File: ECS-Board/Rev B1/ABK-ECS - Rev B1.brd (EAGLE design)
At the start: 100 x 100 mm, 298 parts, among them J1 USB-B-S-RA, J10 FTSH-105-01-L-DV-NOPASTE, J11 22-05-7028-02, J12 RB1-125BAG1A, J13 22-05-7068-06, J14 22-05-7048-04, J15 22-05-7048-04, J16 22-05-7048-04, J2 MSTBA2, J3 22-05-7068-06, J5 22-05-7068-06, J6 22-05-7068-06, J7 22-05-7068-06, J8 22-05-7028-02, J9 FTSH-103-01-L-DV-NOPASTE, SW1 B3FS-1015, SW2 B3FS-1015, T1 MMBT2907ALT3, T10 MMBT2222AL, T11 IRLML5103TRPBF, T12 MMBT2222AL, T13 IRLML5103TRPBF, T14 IRLML5103TRPBF, T15 IRLML5103TRPBF, T16 IRLML5103TRPBF, T17 MMBT2222AL, T18 MMBT2222AL, T19 MMBT2222AL, T2 EXMACHINA-LOGO-NAME, T20 MMBT2222AL, T3 IRLML5103TRPBF, T4 IRLML5103TRPBF, T5 IRLML5103TRPBF, T6 IRLML5103TRPBF, T7 MMBT2222AL, T8 MMBT2222AL, T9 MMBT2222AL, U1 AT24C512C-SSHM-B, U10 SN74LVC2G17DBVR, U2 LPC1768FBD100, U3 LT3686HDDPBF, U4 LT3686HDDPBF, U5 CD4050BD, U6 CD4050BD, U7 DP83848JSQ/NOPB, U9 SN74LVC2G17DBVR, X1 FC-135, X2 ASE-12, X3 3000, X4 ASE_50

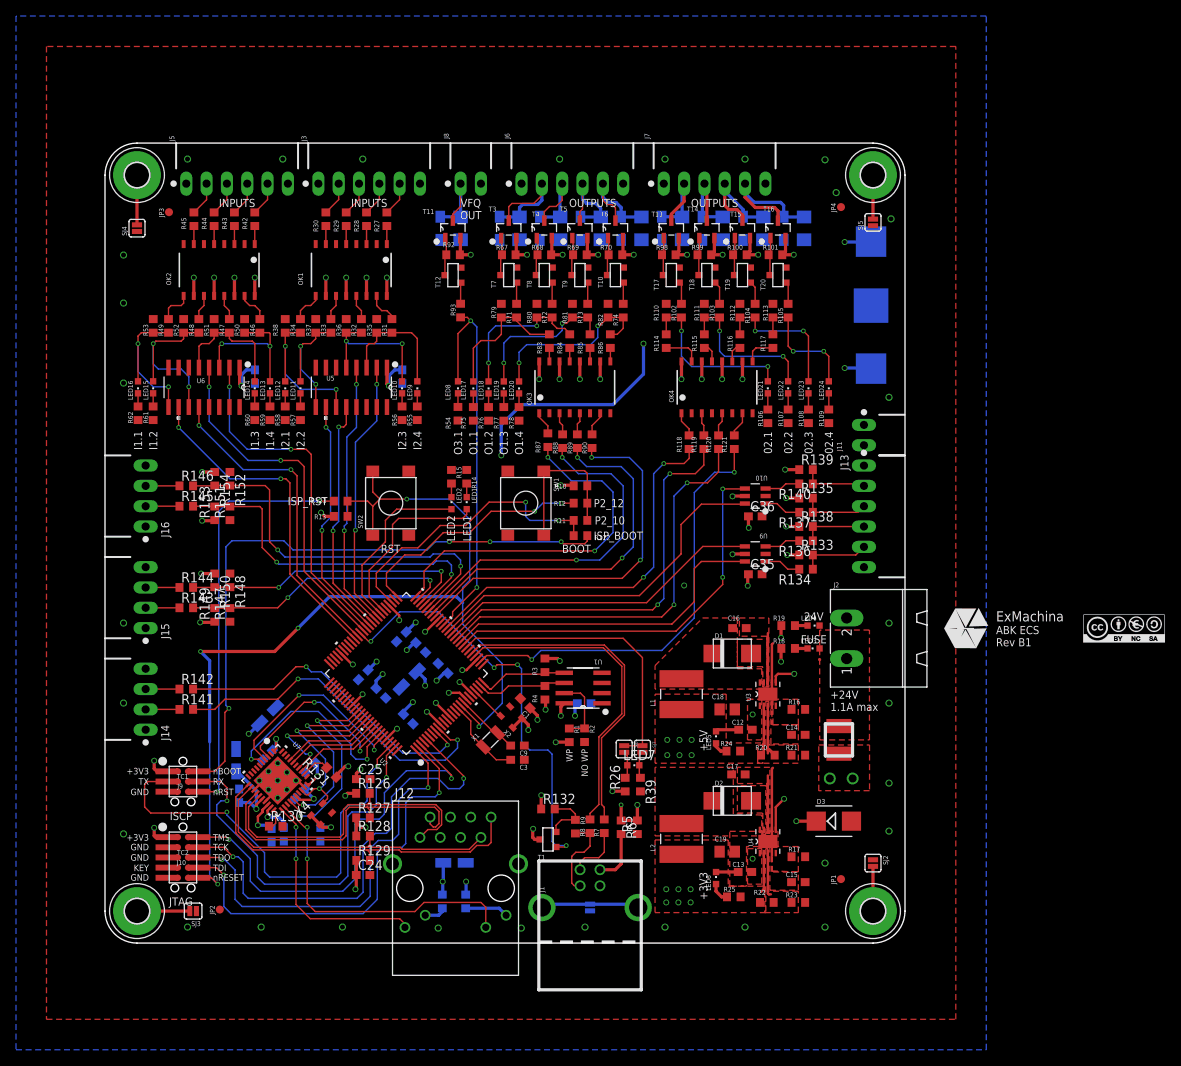
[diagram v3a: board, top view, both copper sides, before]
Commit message: Improte routing and add Silkscreen
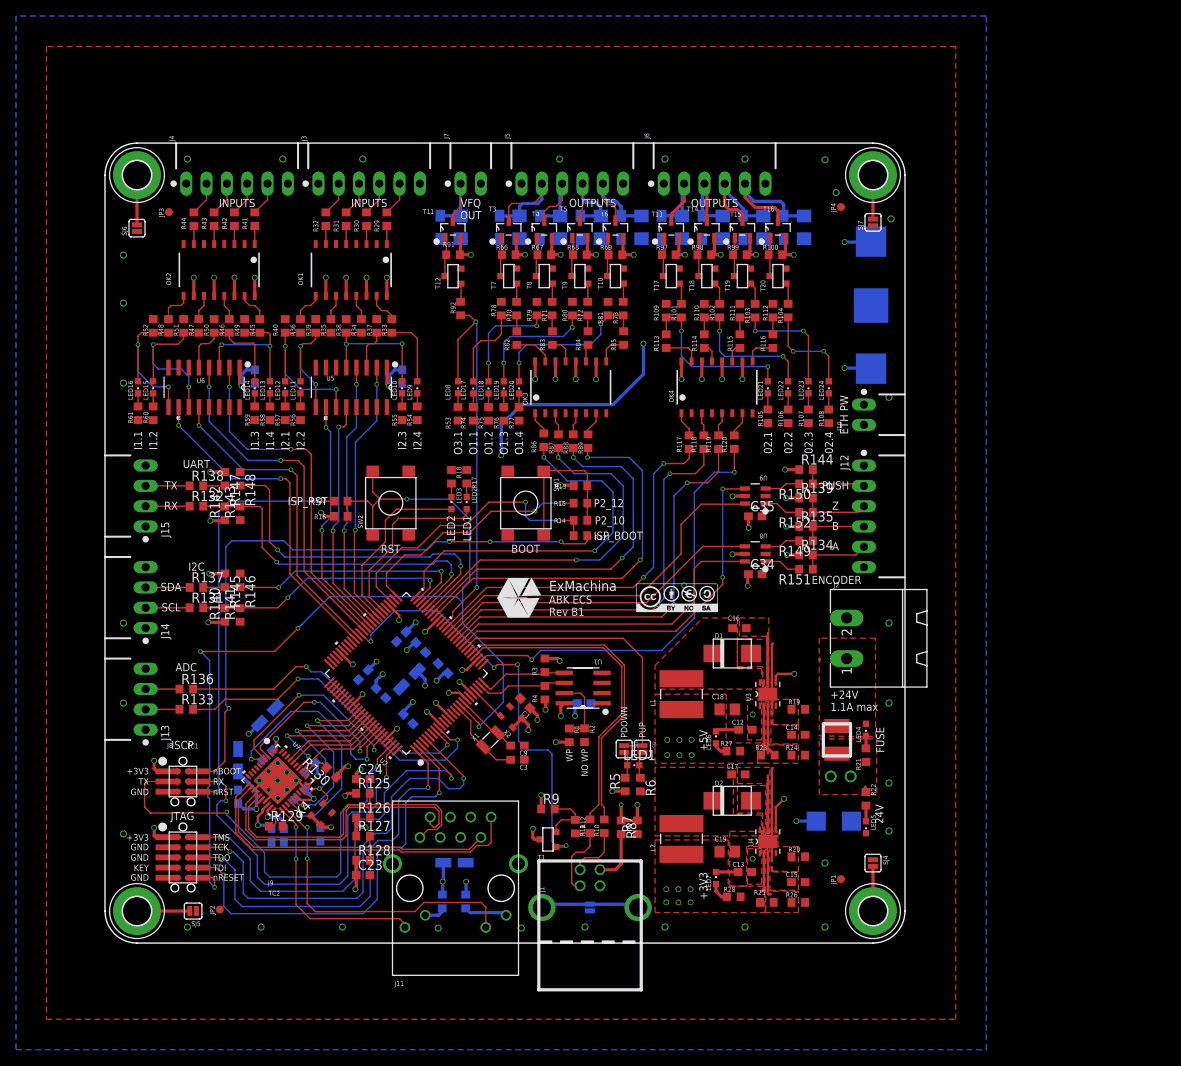
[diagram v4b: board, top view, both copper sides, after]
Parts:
- removed C36: 0.1uF, rcl:C0603
- removed D13: 1N4148WS, diode:SOD323-W
- removed J16: 22-05-7048-04, con-molex:7395-04
- removed R153, R154: 1K, rcl:R0603
- removed U10: SN74LVC2G17DBVR, ti:SOT95P280X145-6N
- added C20: 0.1uF, rcl:C0603
- added D4: 1N4148WS, diode:SOD323-W
- added J4: 22-05-7068-06, con-molex:7395-06
- added R40: 4K7, rcl:R0603
- added R41: 1K, rcl:R0603
- added U8: SN74LVC2G17DBVR, ti:SOT95P280X145-6N
- C22: value 0.1uF -> 4.7uF; device rcl:C0603 -> rcl:CT3216
- C23: value 4.7uF -> 100nF; device rcl:CT3216 -> rcl:C0603
- C25, C29: value 100nF -> 10uF; device rcl:C0603 -> rcl:CT3216
- C26, C30: value 10uF -> 100nF; device rcl:CT3216 -> rcl:C0603
- C34: value 100nF -> 0.1uF
- J10: value FTSH-105-01-L-DV-NOPASTE -> 22-05-7028-02; device con-samtec:FTSH-105-01-L-DV-NOPASTE -> con-molex:7395-02
- J11: value 22-05-7028-02 -> RB1-125BAG1A; device con-molex:7395-02 -> con-wiznet:WIZNET_RB1-125BAG1A
- J12: value RB1-125BAG1A -> 22-05-7068-06; device con-wiznet:WIZNET_RB1-125BAG1A -> con-molex:7395-06
- J13: value 22-05-7068-06 -> 22-05-7048-04; device con-molex:7395-06 -> con-molex:7395-04
- J7: value 22-05-7068-06 -> 22-05-7028-02; device con-molex:7395-06 -> con-molex:7395-02
- J8: value 22-05-7028-02 -> FTSH-103-01-L-DV-NOPASTE; device con-molex:7395-02 -> con-samtec:FTSH-103-01-L-DV-NOPASTE
- J9: value FTSH-103-01-L-DV-NOPASTE -> FTSH-105-01-L-DV-NOPASTE; device con-samtec:FTSH-103-01-L-DV-NOPASTE -> con-samtec:FTSH-105-01-L-DV-NOPASTE
- LED3: value Red -> Blue
- LED4: value Blue -> Red
- MP1, MP2, MP3, MP4: value MOUNT-PAD3,0 -> MOUNT-PAD3.5; device holes:P3,0 -> holes:P3,5
- R10: value 10K -> 33
- R101, R70: value 10K -> 1K
- R105, R27, R28, R74: value 1K -> 1K5
- R109, R39, R78: value 1K5 -> 4K7
- R11: value 0R -> 33
- R113, R82: value 4K7 -> 100
- R117, R86: value 100 -> 330
- R12: value 0R -> 1K5
- R121: value 330 -> 0R
- R123: value 0R -> 220
- R125: value 220 -> 49.9
- R129: value 49.9 -> 4K7
- R130: value 4K7 -> 2K2
- R131: value 2K2 -> 1K
- R132: value 0R, DNI -> 1K
- R133, R138, R35, R36: value 4K7 -> 1K
- R134, R144, R49: value 1K -> 4K7
- R14, R15: value 1K5 -> 0R
- R16: value 31K6 -> 10K
- R17: value 31K6 -> 1K5
- R18, R53: value 4K7 -> 1K5
- R19: value 4K7 -> 31K6
- R20: value 52K3 -> 31K6
- R21: value 10K -> 4K7
- R22: value 31K6 -> 4K7
- R23: value 10K -> 52K3
- R24, R26: value 1K5 -> 10K
- R25: value 1K5 -> 31K6
- R5: value 39K -> 1K5
- R6: value 24K -> 1K5
- R62: value 1K5 -> 1K; device rcl:R0603 -> rcl:R1206
- R66, R91, R97: value 1K -> 10K; device rcl:R1206 -> rcl:R0603
- R7: value 33 -> 39K
- R8: value 33 -> 24K
- R9: value 1K5 -> 0R, DNI
- R90: value 330 -> 1K; device rcl:R0603 -> rcl:R1206
- R92: value 10K -> 100
- R93: value 100 -> 1K; device rcl:R0603 -> rcl:R1206
- SJ1: value (none) -> SJNC
- SJ2, SJ3, SJ4, SJ5: value SOLDERJUMPERNC -> SJNC
- moved SJ4 121.5 mm to (96.0, 10.0), turned to 270 degrees
- moved SJ5 121.0 mm to (11.0, 4.00), turned to 180 degrees
- moved J10 101.5 mm to (94.9, 66.0), turned to 90 degrees
- moved R28 96.3 mm to (78.6, 5.78), turned to 0 degrees
- moved J13 92.7 mm to (5.08, 30.5), turned to 270 degrees
- moved SJ6 89.1 mm to (4.00, 89.4), turned to 90 degrees
- moved J8 82.9 mm to (9.74, 20.2), turned to 270 degrees
- moved R133 79.8 mm to (10.2, 29.2)
- moved R136 79.7 mm to (10.2, 31.8), turned to 0 degrees
- moved R27 79.3 mm to (78.5, 24.0), turned to 0 degrees
- moved R144 78.9 mm to (87.6, 59.2)
- moved R137 76.8 mm to (11.4, 44.5), turned to 0 degrees
- moved R138 76.4 mm to (11.4, 57.1)
- moved J11 76.3 mm to (43.8, 6.86), turned to 0 degrees
- moved R150 74.9 mm to (87.6, 57.4), turned to 180 degrees
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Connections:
- removed net N$3 (its old number): LED2.C, R15.1
- new net N$45: LED4.C, R21.1
- net !ISP_BOOT: now also J8.2, R121.2; no longer J9.2, R122.2
- net !ISP_RST: now also J8.6, R122.2; no longer J9.6, R123.2
- net !RESET: now also J9.10, R122.1, R16.1; no longer J10.10, R123.1, R13.1
- net +24V: now also J4.1, R21.2, R22.2, R66.2, R91.2, R97.2; no longer J7.1, R101.2, R18.2, R19.2, R70.2, R92.2
- net +3V3: now also C20.1, C22.+, C23.1, C29.+, C30.1, J11.R3, J14.1, J8.1, R123.2, R125.1, R130.1, R140.1, R142.1, R145.1, R147.1, R16.2, R28.2, R5.1, R9.1, U8.5; no longer C22.1, C23.+, C25.1, C30.+, C36.1, J10.1, J12.R3, J16.1, R10.2, R125.2, R129.1, R131.1, R132.1, R149.1, R150.1, R153.1, R154.1, R22.2, R26.1, U10.5
- net +5V: now also J10.1, J12.1, R134.1, R144.1, R23.2, R27.2; no longer J11.1, J13.6, R133.1, R138.1, R20.2, R24.2
- net 1: now also SJ4.2; no longer SJ2.2
- net 2: now also SJ5.2; no longer SJ3.2
- net 3: now also SJ6.2; no longer SJ4.2
- net 4: now also SJ7.2; no longer SJ5.2
- net ADC1: now also R136.2; no longer R142.2
- net ADC2: now also R133.2; no longer R141.2
- net AGND: now also J11.S1, J11.S2; no longer J12.S1, J12.S2
- net BOOT_SELECT_P2_10: now also R121.1, R14.1; no longer R11.1, R122.1
- net BOOT_SELECT_P2_12: now also R15.1; no longer R12.1
- net ENCODER_A: now also U8.6; no longer U9.6
- net ENCODER_B: now also U8.4; no longer U9.4
- net ENCODER_PUSH: now also U9.4; no longer U10.4
- net ENCODER_Z: now also U9.6; no longer U10.6
- net ETH_RX_N: now also J11.R8, R128.2; no longer J12.R8, R129.2
- net ETH_RX_P: now also J11.R7, R127.2; no longer J12.R7, R128.2
- net ETH_TX_N: now also J11.R2, R126.2; no longer J12.R2, R127.2
- net ETH_TX_P: now also J11.R1, R125.2; no longer J12.R1, R126.2
- net GND: now also C20.2, C22.-, C23.2, C25.-, C26.2, C29.-, C30.2, D4.A, J10.2, J11.R4, J11.R5, J11.R6, J12.6, J13.4, J4.6, J7.2, J8.5, J9.3, J9.7, J9.9, LED7.C, R105.2, R129.2, R141.1, R143.1, R146.1, R17.2, R18.2, R19.1, R20.1, R24.1, R26.1, R40.2, R49.2, R6.2, R62.1, R7.1, R74.2, R90.1, R93.1, SJ6.1, SJ7.1, U8.2; no longer C22.2, C23.-, C25.2, C26.-, C29.2, C30.-, C36.2, D13.A, J10.3, J10.5, J10.7, J10.9, J11.2, J12.R4, J12.R5, J12.R6, J13.1, J16.4, J7.6, J8.2, LED4.C, R113.2, R130.2, R14.2, R147.1, R15.2, R151.1, R152.1, R16.1, R17.1, R21.1, R23.1, R35.2, R36.2, R5.1, R62.2, R66.1, R82.2, R91.1, R97.1, SJ1.1, SJ2.1, U10.2
- net I2C_SCL: now also R131.2, R140.2, R141.2; no longer R143.2, R147.2, R149.2
- net I2C_SDA: now also R137.2, R145.2, R146.2; no longer R144.2, R148.2, R150.2
- net INPUT1.1: now also R48.2, R52.1; no longer R49.2, R53.1
- net INPUT1.2: now also R47.2, R51.1; no longer R48.2, R52.1
- net INPUT1.3: now also R46.2, R50.1; no longer R47.2, R51.1
- net INPUT1.4: now also R45.2, R49.1; no longer R46.2, R50.1
- net INPUT2.1: now also R36.2, R40.1; no longer R34.2, R38.1
- net INPUT2.2: now also R35.2, R39.1; no longer R33.2, R37.1
- net INPUT2.3: now also R34.2, R38.1; no longer R32.2, R36.1
- net INPUT2.4: now also R33.2, R37.1; no longer R31.2, R35.1
- net ISP_RXDO: now also J8.4; no longer J9.4
- net ISP_TXDO: now also J8.3; no longer J9.3
- net JTAG_TCK: now also J9.4; no longer J10.4
- net JTAG_TDI: now also J9.8; no longer J10.8
- net JTAG_TDO: now also J9.6; no longer J10.6
- net JTAG_TMS: now also J9.2; no longer J10.2
- net L1_1: now also J11.L2; no longer J12.L2
- net L1_2: now also J11.L4; no longer J12.L4
- net MII_MODE: now also R130.2; no longer R131.2
- net MOTOR_VFQ: now also D8.C, J7.1, R90.2; no longer D9.C, J8.1, R91.2
- net N$1: now also R11.1, R12.2; no longer R8.1, R9.2
- net N$100: now also R45.1; no longer R46.1
- net N$101: now also R42.2; no longer R43.2
- net N$102: now also J4.4, R42.1; no longer J5.4, R43.1
- net N$103: now also R46.1; no longer R47.1
- net N$104: now also R43.2; no longer R44.2
- net N$105: now also J4.3, R43.1; no longer J5.3, R44.1
- net N$106: now also R47.1; no longer R48.1
- net N$107: now also R58.1; no longer R59.1
- net N$108: now also R59.1; no longer R60.1
- net N$109: now also R60.1; no longer R61.1
- net N$110: now also R48.1; no longer R49.1
- net N$111: now also R44.2; no longer R45.2
- net N$112: now also J4.2, R44.1; no longer J5.2, R45.1
- net N$113: now also J11.L1, R123.1; no longer J12.L1, R124.1
- net N$114: now also R8.2; no longer R6.2
- net N$115: now also J11.L3, R124.1; no longer J12.L3, R125.1
- net N$116: now also R129.1; no longer R130.1
- net N$117: now also J12.5, R134.2, R151.1; no longer J13.5, R133.2, R134.1
- net N$118: now also J12.4, R135.2, R149.1; no longer J13.4, R136.1, R138.2
- net N$119: now also J12.3, R139.2, R152.1; no longer J13.3, R135.2, R137.1
- net N$120: now also R150.2, U9.3; no longer R140.2, U10.3
- net N$121: now also R149.2, U8.3; no longer R136.2, U9.3
- net N$122: now also R151.2, U8.1; no longer R134.2, U9.1
- net N$123: now also R152.2, U9.1; no longer R137.2, U10.1
- net N$124: now also J12.2, R144.2, R150.1; no longer J13.2, R139.2, R140.1
- net N$125: now also J13.2, R133.1; no longer J14.2, R141.1
- net N$126: now also J13.3, R136.1; no longer J14.3, R142.1
- net N$127: now also J14.2, R131.1; no longer J15.2, R143.1
- net N$128: now also J14.3, R137.1; no longer J15.3, R144.1
- net N$129: now also J15.2, R132.1; no longer J16.2, R145.1
- net N$13: now also R25.1, R26.2; no longer R22.1, R23.2
- net N$130: now also J15.3, R138.1; no longer J16.3, R146.1
- net N$17: now also R101.2; no longer R102.2
- net N$18: now also R97.1; no longer R98.1
- net N$19: now also R102.2; no longer R103.2
- net N$2: now also R10.1; no longer R7.1
- net N$20: now also R98.1; no longer R99.1
- net N$21: now also R103.2; no longer R104.2
- net N$22: now also R99.1; no longer R100.1
- net N$23: now also R104.2; no longer R105.2
- net N$24: now also R100.1; no longer R101.1
- net N$25: now also R92.1; no longer R93.1
- net N$26: now also R91.1; no longer R92.1
- net N$28: now also LED1.A, R5.2, SJ1.2; no longer LED7.A, R26.2, SJ6.2
- net N$29: now also LED2.C, R17.1; no longer LED1.C, R14.1
- net N$30: now also R12.1, R9.2; no longer R132.2, R9.1
- net N$31: now also R70.1, R78.1, R82.1; no longer R71.1, R79.1, R83.1
- net N$32: now also LED1.C, R6.1, SJ2.2; no longer LED7.C, R39.1, SJ7.2
- net N$33: now also R82.2; no longer R83.2
- net N$34: now also R71.1, R79.1, R83.1; no longer R72.1, R80.1, R84.1
- net N$35: now also R83.2; no longer R84.2
- net N$36: now also R72.1, R80.1, R84.1; no longer R73.1, R81.1, R85.1
- net N$37: now also R73.1, R81.1, R85.1; no longer R74.1, R82.1, R86.1
- net N$38: now also R84.2; no longer R85.2
- net N$39: now also R85.2; no longer R86.2
- net N$4: now also R19.2; no longer R16.2
- net N$40: now also R86.1; no longer R87.1
- net N$41: now also R29.2; no longer R27.2
- net N$42: now also R87.1; no longer R88.1
- net N$43: now also R89.1; no longer R90.1
- net N$44: now also LED5.A, R22.1; no longer LED4.A, R19.1
- net N$46: now also R88.1; no longer R89.1
- net N$47: now also R30.2; no longer R28.2
- net N$48: now also R31.2; no longer R29.2
- net N$49: now also R32.2; no longer R30.2
- net N$5: now also R13.1, R14.2, R15.2; no longer R10.1, R11.2, R12.2
- net N$50: now also LED7.A, R28.1; no longer LED6.A, R25.1
- net N$51: now also LED6.A, R27.1; no longer LED5.A, R24.1
- net N$52: now also R32.1; no longer R30.1
- net N$53: now also R31.1; no longer R29.1
- net N$54: now also R30.1; no longer R28.1
- net N$55: now also R29.1; no longer R27.1
- net N$56: now also R53.1; no longer R54.1
- net N$57: now also R54.1; no longer R55.1
- net N$58: now also R55.1; no longer R56.1
- net N$59: now also R56.1; no longer R57.1
- net N$61: now also R36.1; no longer R34.1
- net N$62: now also R35.1; no longer R33.1
- net N$63: now also R34.1; no longer R32.1
- net N$64: now also R33.1; no longer R31.1
- net N$65: now also R57.1; no longer R58.1
- net N$66: now also R74.1; no longer R75.1
- net N$67: now also R75.1; no longer R76.1
- net N$68: now also R76.1; no longer R77.1
- net N$69: now also R77.1; no longer R78.1
- net N$7: now also R20.2; no longer R17.2
- net N$70: now also SJ3.2; no longer SJ1.2
- net N$71: now also R66.1; no longer R67.1
- net N$72: now also R67.1; no longer R68.1
- net N$75: now also R101.1, R109.1, R113.1; no longer R102.1, R110.1, R114.1
- net N$76: now also R113.2; no longer R114.2
- net N$77: now also R68.1; no longer R69.1
- net N$78: now also R69.1; no longer R70.1
- net N$79: now also R102.1, R110.1, R114.1; no longer R103.1, R111.1, R115.1
- net N$80: now also R114.2; no longer R115.2
- net N$81: now also R41.2; no longer R42.2
- net N$82: now also J4.5, R41.1; no longer J5.5, R42.1
- net N$83: now also R103.1, R111.1, R115.1; no longer R104.1, R112.1, R116.1
- net N$84: now also R70.2; no longer R71.2
- net N$85: now also R71.2; no longer R72.2
- net N$86: now also R104.1, R112.1, R116.1; no longer R105.1, R113.1, R117.1
- net N$87: now also R115.2; no longer R116.2
- net N$88: now also R116.2; no longer R117.2
- net N$89: now also R117.1; no longer R118.1
- net N$9: now also R23.1, R24.2; no longer R20.1, R21.2
- net N$90: now also R61.1; no longer R62.1
- net N$91: now also R118.1; no longer R119.1
- net N$92: now also R120.1; no longer R121.1
- net N$93: now also R119.1; no longer R120.1
- net N$94: now also R105.1; no longer R106.1
- net N$95: now also R106.1; no longer R107.1
- net N$96: now also R107.1; no longer R108.1
- net N$97: now also R108.1; no longer R109.1
- net N$98: now also R72.2; no longer R73.2
- net N$99: now also R73.2; no longer R74.2
- net ONBOARD_LED1: now also LED3.A; no longer LED2.A
- net ONBOARD_LED2: now also LED2.A; no longer LED1.A
- net OUTPUT1.1: now also D4.C, J5.2, R62.2; no longer D5.C, J6.2, R63.2
- net OUTPUT1.1_MCU: now also R86.2; no longer R87.2
- net OUTPUT1.2: now also D5.C, J5.3, R63.2; no longer D6.C, J6.3, R64.2
- net OUTPUT1.2_MCU: now also R87.2; no longer R88.2
- net OUTPUT1.3: now also D6.C, J5.4, R64.2; no longer D7.C, J6.4, R65.2
- net OUTPUT1.3_MCU: now also R88.2; no longer R89.2
- net OUTPUT1.4: now also D7.C, J5.5, R65.2; no longer D8.C, J6.5, R66.2
- net OUTPUT1.4_MCU: now also R89.2; no longer R90.2
- net OUTPUT2.1: now also D9.C, J6.2, R93.2; no longer D10.C, J7.2, R94.2
- net OUTPUT2.1_MCU: now also R117.2; no longer R118.2
- net OUTPUT2.2: now also D10.C, J6.3, R94.2; no longer D11.C, J7.3, R95.2
- net OUTPUT2.2_MCU: now also R118.2; no longer R119.2
- net OUTPUT2.3: now also D11.C, J6.4, R95.2; no longer D12.C, J7.4, R96.2
- net OUTPUT2.3_MCU: now also R119.2; no longer R120.2
- net OUTPUT2.4: now also D12.C, J6.5, R96.2; no longer D13.C, J7.5, R97.2
- net OUTPUT2.4_MCU: now also R120.2; no longer R121.2
- net OUTPUT3.2_MCU: now also R92.2; no longer R93.2
- net PFBOUT: now also C25.+, C26.1; no longer C26.+, C29.1
- net UART_RX: now also R132.2, R142.2, R143.2; no longer R145.2, R151.2, R153.2
- net UART_TX: now also R138.2, R147.2, R148.2; no longer R146.2, R152.2, R154.2
- net USB_D_N: now also R10.2; no longer R7.2
- net USB_D_P: now also R11.2; no longer R8.2
- net USB_LED: now also SJ1.1, SJ2.1; no longer SJ6.1, SJ7.1
- net USB_V_BUS: now also R7.2, R8.1; no longer R5.2, R6.1
- net VIN: now also LED4.A; no longer LED3.A
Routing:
- net +24V: track 46.8 -> 42.9 mm, vias 18 -> 16
- net N$33: track 1.69 -> 4.86 mm
- net N$31: track 17.6 -> 14.6 mm
- net N$39: track 1.69 -> 3.90 mm
- net N$35: track 1.69 -> 3.41 mm
- net N$3 (its old number): track 1.70 -> 0.00 mm
- net N$45: track 0.00 -> 1.58 mm
- net N$34: track 19.1 -> 17.7 mm
- net UART_RX: track 44.9 -> 43.6 mm
- net I2C_SDA: track 36.8 -> 35.5 mm
- net UART_TX: track 49.1 -> 47.9 mm
- net N$130: track 4.23 -> 5.50 mm
- net N$129: track 4.23 -> 5.50 mm
- net N$128: track 4.23 -> 5.50 mm
- net N$127: track 4.23 -> 5.50 mm
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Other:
- board text added: "A"
- board text added: "ADC"
- board text added: "B"
- board text added: "ENCODER"
- board text added: "ETH PW"
- board text added: "I2C"
- board text added: "PDOWN"
- board text added: "PUP"
- board text added: "PUSH"
- board text added: "SCL"
- board text added: "SDA"
- board text added: "UART"
- board text added: "Z"

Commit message: Final changes before manufacturing:
- Update silkscreen:
  * Place labels for each pin
  * Update USB silkscreen
  * Update RJ45 silkscreen
  * Update +24V socket silkscreen
  * Update battery holder silscreen
- Remove useless solder jumpers for USB_UP_LED
- Update the guard ring vias
- Enlarge +24V plane
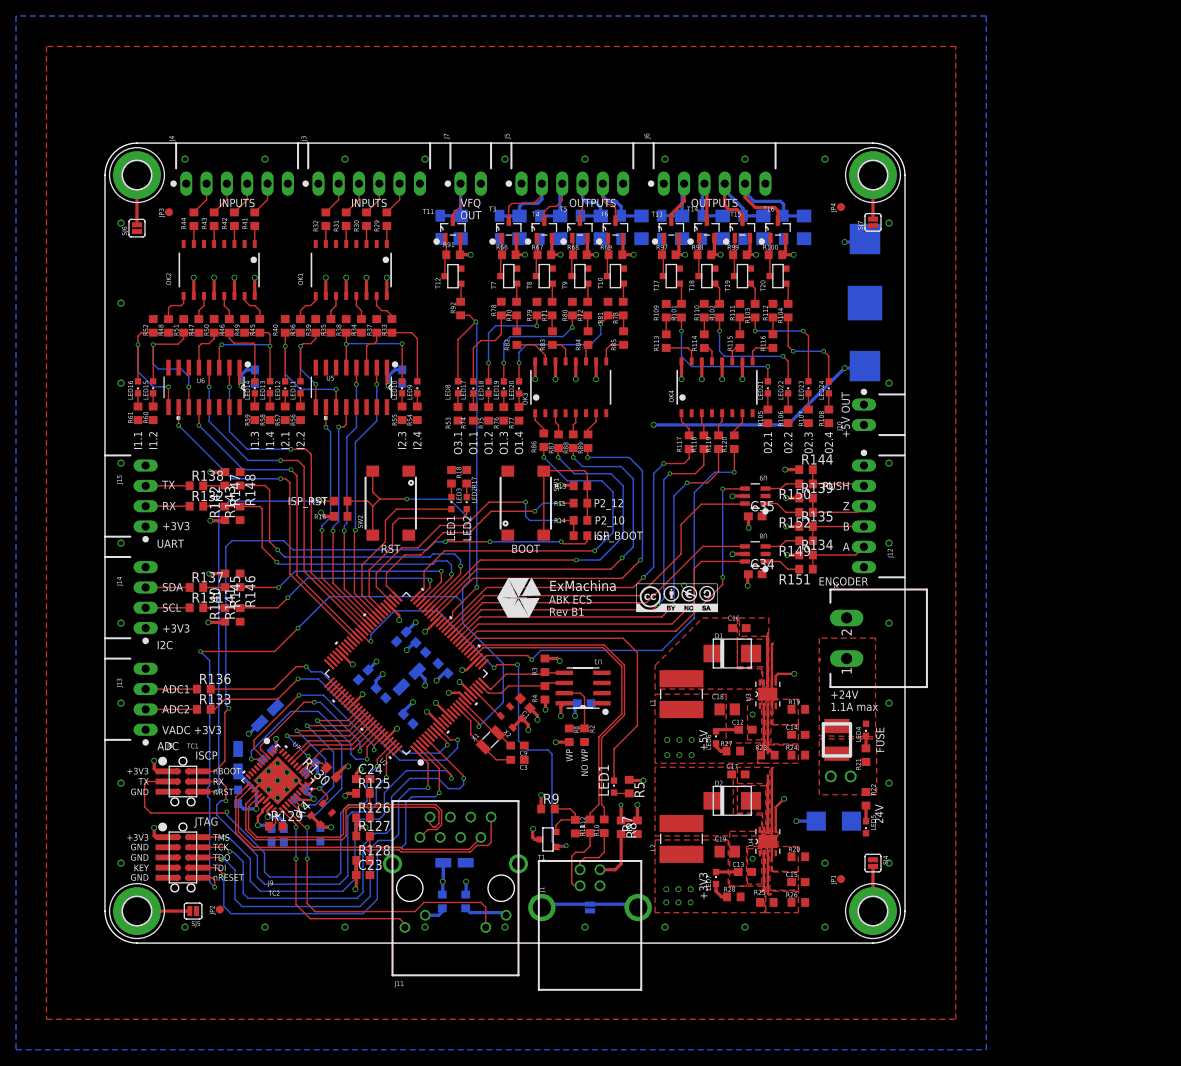
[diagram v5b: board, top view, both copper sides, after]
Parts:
- removed R6: 1K5, rcl:R0603
- removed SJ1, SJ2: SJNC, SparkFun-Passives:SJ_2S
- moved LED1 3.60 mm to (63.6, 19.6), turned to 0 degrees
- moved R133 2.20 mm to (12.4, 29.2)
- moved R136 2.20 mm to (12.4, 31.8)
- moved X3 0.82 mm to (95.0, 80.0)
- moved R5 0.57 mm to (65.5, 19.6), turned to 270 degrees
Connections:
- removed net N$32: LED1.C, R6.1, SJ2.2
- net GND: no longer R6.2
- net N$28: no longer SJ1.2
- net USB_LED: now also LED1.C; no longer SJ1.1, SJ2.1
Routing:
- net VBAT+: track 113.8 -> 103.5 mm, vias 5 -> 4
- net N$32: track 3.40 -> 0.00 mm
- net USB_LED: track 36.8 -> 39.8 mm
- net ADC1: track 40.2 -> 38.0 mm
- net N$126: track 4.23 -> 6.43 mm
- net N$125: track 4.23 -> 6.43 mm
- net ADC2: track 43.5 -> 41.3 mm
- net N$28: track 3.46 -> 1.95 mm
- net +24V: track 42.9 -> 41.8 mm
- net GND: vias 40 -> 46
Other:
- board text added: "+5V OUT"
- board text added: "ADC1"
- board text added: "ADC2"
- board text added: "VADC +3V3"
- board text removed: "ETH PW"
- board text removed: "PDOWN"
- board text removed: "PUP"
